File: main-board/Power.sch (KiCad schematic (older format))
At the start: 55 parts, among them J4 5V Input, Q1 N Channel, Q10 N Channel, Q11 N Channel, Q12 N Channel, Q13 P Channel, Q14 P Channel, Q15 P Channel, Q16 P Channel, Q17 P Channel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

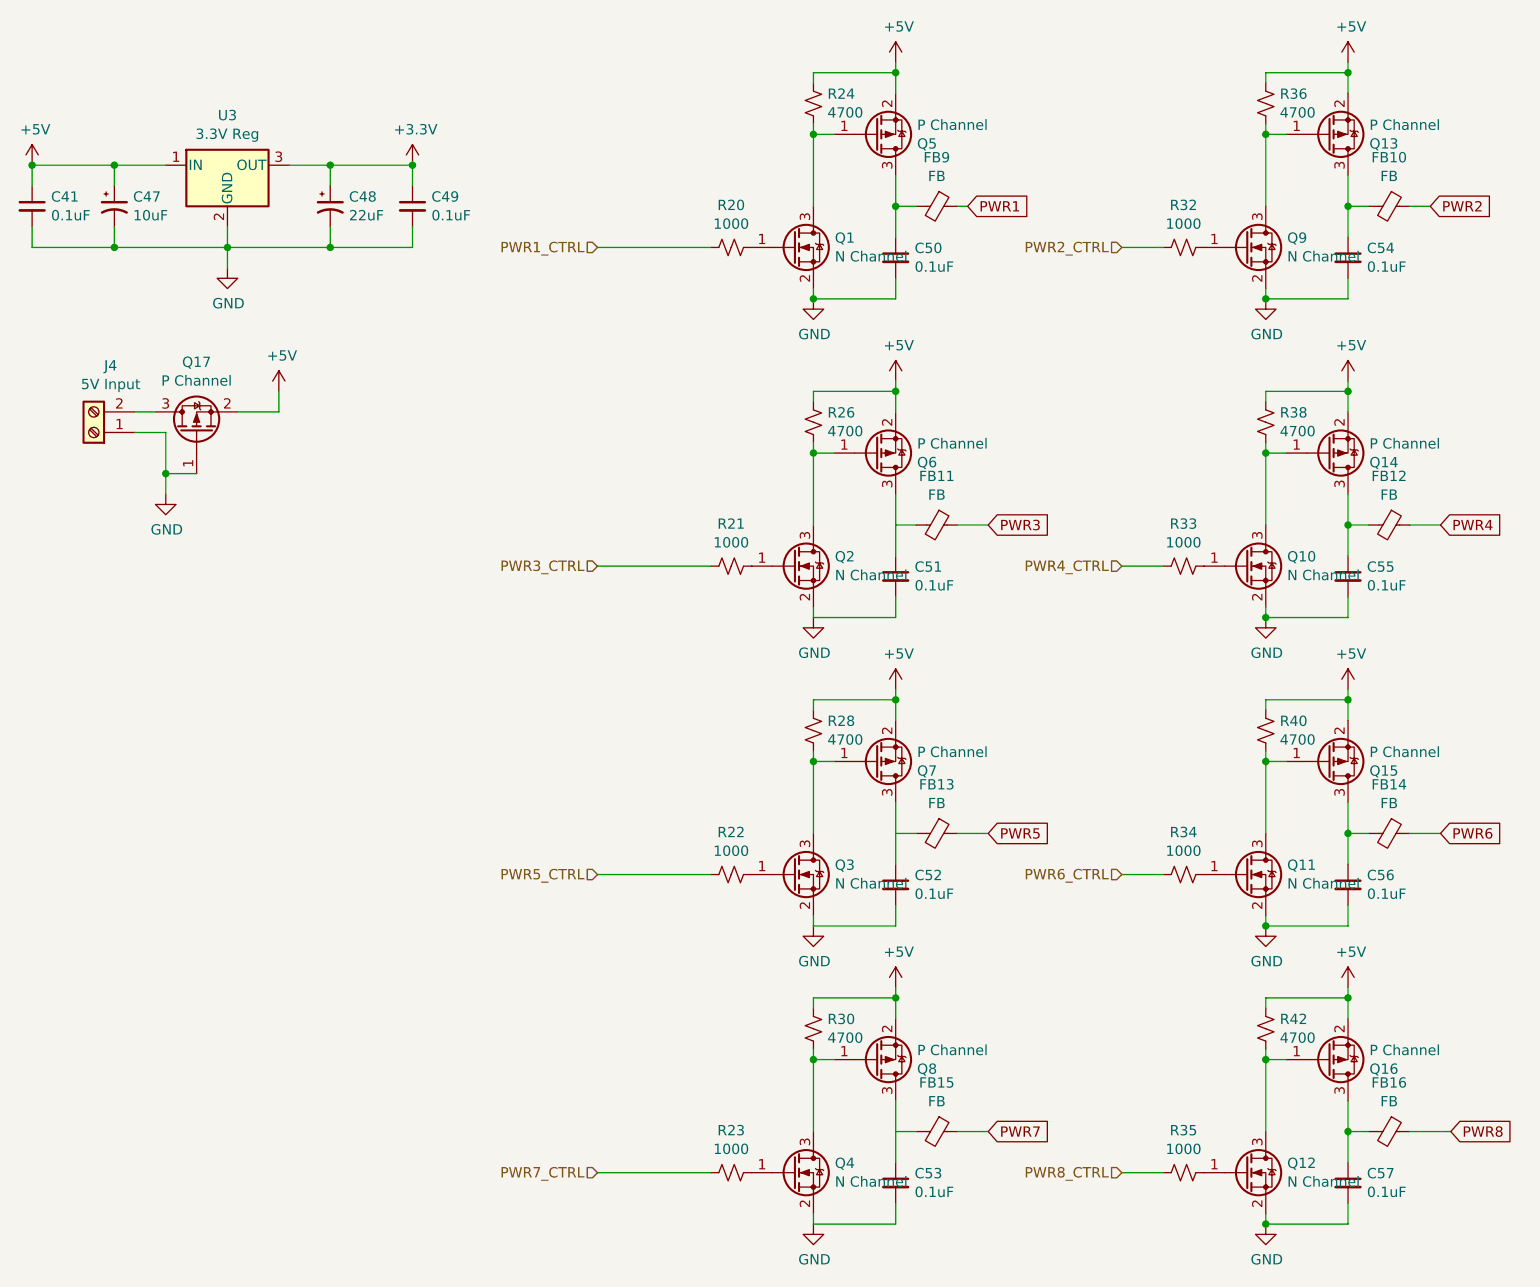
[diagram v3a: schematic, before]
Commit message: First round of rev 1 changes. This was a complete relayout.
* RS485 transceiver footprint fixed
* Compressed board to 100x100mm exactly
* Removed ethernet
* Changed FET footprints to SOT-23
* Swapped USB D+/D- to correct positions
* Spaced out +5V and GND silkscreen on power input
* Added JLCPCB order number silkscreen
* Spaced out Qwiic headers
* Added some more space around 3.3V regulator.
* Slightly increased size of electrolytic caps.
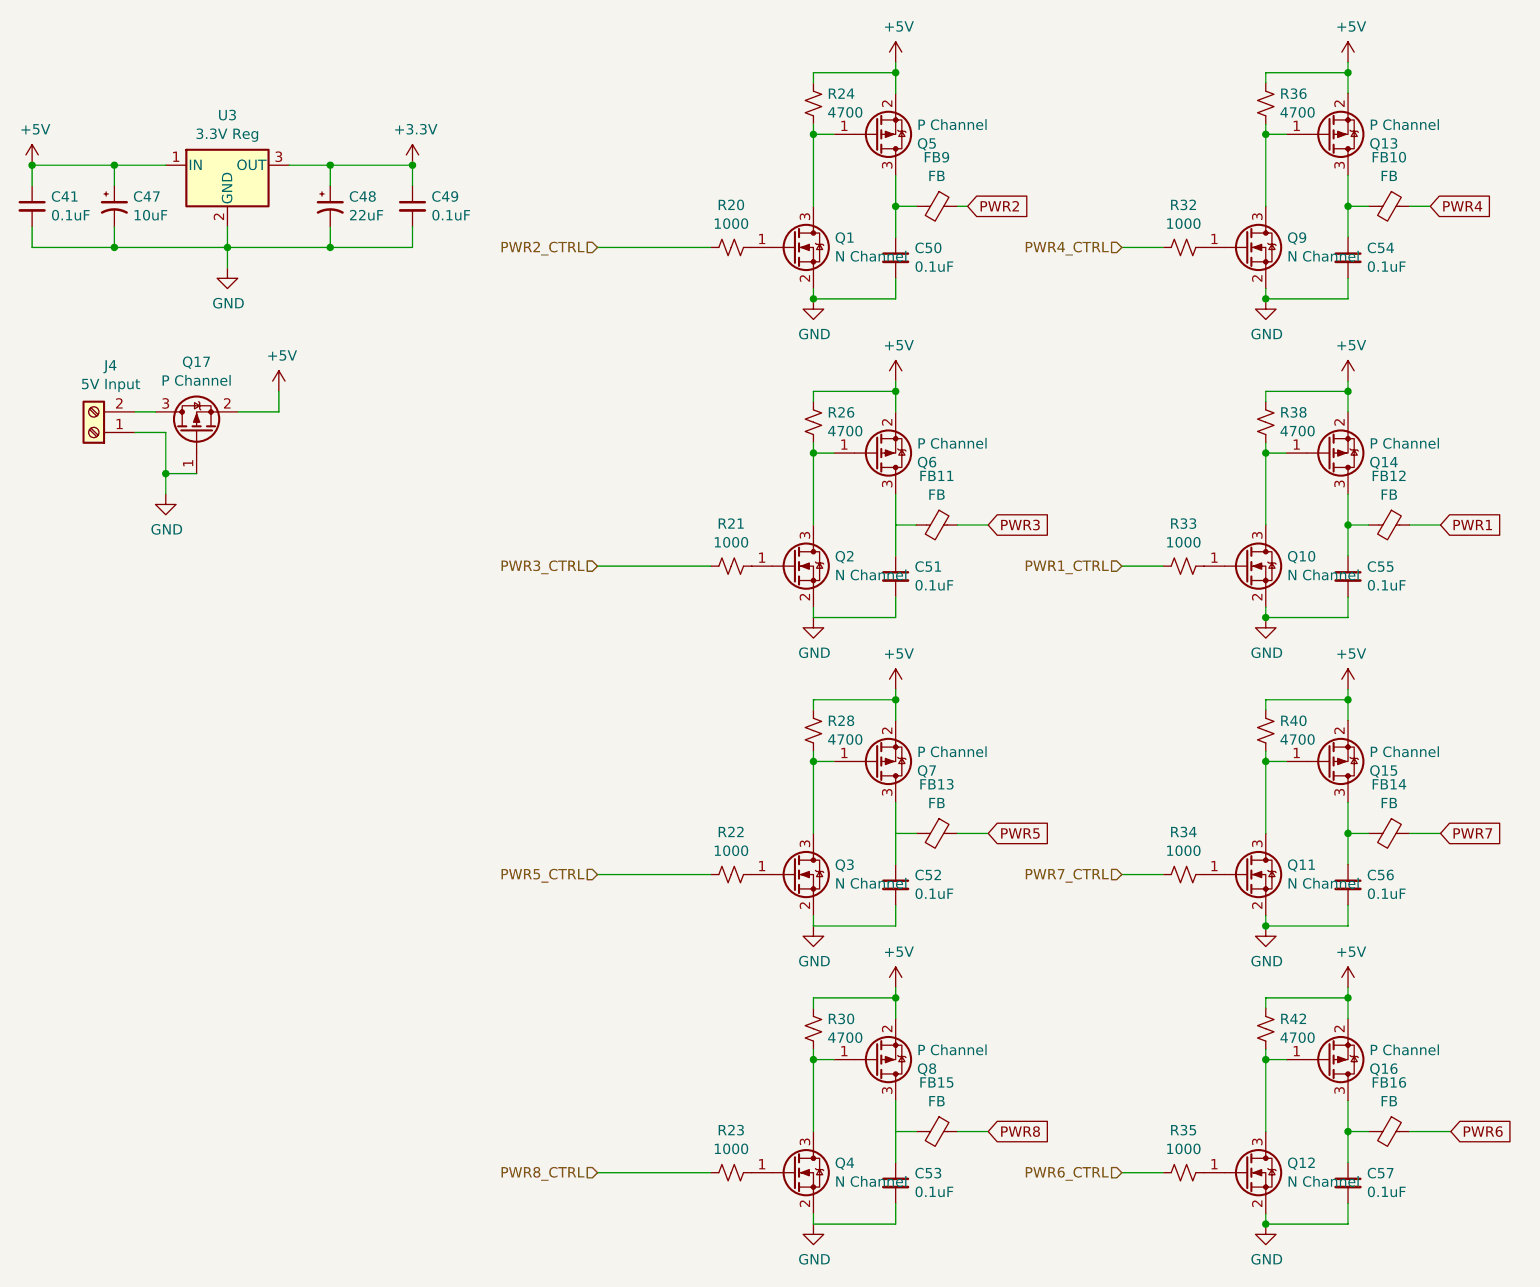
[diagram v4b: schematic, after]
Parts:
- C47: footprint Capacitors_SMD:CP_Elec_4x4.5 -> Capacitors_SMD:CP_Elec_5x5.3
- C48: footprint Capacitors_SMD:CP_Elec_5x5.3 -> Capacitors_SMD:CP_Elec_6.3x5.8
- Q1, Q10, Q11, Q12, Q13, Q14, Q15, Q16, Q17, Q2, Q3, Q4, Q5, Q6, Q7, Q8, Q9: footprint TO_SOT_Packages_SMD:SOT-323_SC-70_Handsoldering -> TO_SOT_Packages_SMD:SOT-23
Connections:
- net PWR1: now also FB12.1; no longer FB9.1
- net PWR1_CTRL: now also R33.2; no longer R20.2
- net PWR2: now also FB9.1; no longer FB10.1
- net PWR2_CTRL: now also R20.2; no longer R32.2
- net PWR4: now also FB10.1; no longer FB12.1
- net PWR4_CTRL: now also R32.2; no longer R33.2
- net PWR6: now also FB16.1; no longer FB14.1
- net PWR6_CTRL: now also R35.2; no longer R34.2
- net PWR7: now also FB14.1; no longer FB15.1
- net PWR7_CTRL: now also R34.2; no longer R23.2
- net PWR8: now also FB15.1; no longer FB16.1
- net PWR8_CTRL: now also R23.2; no longer R35.2
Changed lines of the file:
@@
 F 0 "C47" H 1341 1596 50  0000 L CNN
 F 1 "10uF" H 1341 1505 50  0000 L CNN
-F 2 "Capacitors_SMD:CP_Elec_4x4.5" H 1250 1550 50  0001 C CNN
+F 2 "Capacitors_SMD:CP_Elec_5x5.3" H 1250 1550 50  0001 C CNN
 F 3 "~" H 1250 1550 50  0001 C CNN
 	1    1250 1550
@@
 F 0 "C48" H 2391 1596 50  0000 L CNN
 F 1 "22uF" H 2391 1505 50  0000 L CNN
-F 2 "Capacitors_SMD:CP_Elec_5x5.3" H 2300 1550 50  0001 C CNN
+F 2 "Capacitors_SMD:CP_Elec_6.3x5.8" H 2300 1550 50  0001 C CNN
 F 3 "~" H 2300 1550 50  0001 C CNN
 	1    2300 1550
@@
 F 0 "Q1" H 4754 1796 50  0000 L CNN
 F 1 "N Channel" H 4754 1705 50  0000 L CNN
-F 2 "TO_SOT_Packages_SMD:SOT-323_SC-70_Handsoldering" H 4750 1850 50  0001 C CNN
+F 2 "TO_SOT_Packages_SMD:SOT-23" H 4750 1850 50  0001 C CNN
 F 3 "~" H 4550 1750 50  0001 C CNN
 	1    4550 1750
@@
 F 0 "Q5" H 5154 1246 50  0000 L CNN
 F 1 "P Channel" H 5154 1155 50  0000 L CNN
-F 2 "TO_SOT_Packages_SMD:SOT-323_SC-70_Handsoldering" H 5150 1300 50  0001 C CNN
+F 2 "TO_SOT_Packages_SMD:SOT-23" H 5150 1300 50  0001 C CNN
 F 3 "~" H 4950 1200 50  0001 C CNN
 	1    4950 1200
@@
 F 0 "Q9" H 6954 1796 50  0000 L CNN
 F 1 "N Channel" H 6954 1705 50  0000 L CNN
-F 2 "TO_SOT_Packages_SMD:SOT-323_SC-70_Handsoldering" H 6950 1850 50  0001 C CNN
+F 2 "TO_SOT_Packages_SMD:SOT-23" H 6950 1850 50  0001 C CNN
 F 3 "~" H 6750 1750 50  0001 C CNN
 	1    6750 1750
@@
 F 0 "Q13" H 7354 1246 50  0000 L CNN
 F 1 "P Channel" H 7354 1155 50  0000 L CNN
-F 2 "TO_SOT_Packages_SMD:SOT-323_SC-70_Handsoldering" H 7350 1300 50  0001 C CNN
+F 2 "TO_SOT_Packages_SMD:SOT-23" H 7350 1300 50  0001 C CNN
 F 3 "~" H 7150 1200 50  0001 C CNN
 	1    7150 1200
@@
 F 0 "Q2" H 4754 3346 50  0000 L CNN
 F 1 "N Channel" H 4754 3255 50  0000 L CNN
-F 2 "TO_SOT_Packages_SMD:SOT-323_SC-70_Handsoldering" H 4750 3400 50  0001 C CNN
+F 2 "TO_SOT_Packages_SMD:SOT-23" H 4750 3400 50  0001 C CNN
 F 3 "~" H 4550 3300 50  0001 C CNN
 	1    4550 3300
@@
 F 0 "Q6" H 5154 2796 50  0000 L CNN
 F 1 "P Channel" H 5154 2705 50  0000 L CNN
-F 2 "TO_SOT_Packages_SMD:SOT-323_SC-70_Handsoldering" H 5150 2850 50  0001 C CNN
+F 2 "TO_SOT_Packages_SMD:SOT-23" H 5150 2850 50  0001 C CNN
 F 3 "~" H 4950 2750 50  0001 C CNN
 	1    4950 2750
@@
 F 0 "Q10" H 6954 3346 50  0000 L CNN
 F 1 "N Channel" H 6954 3255 50  0000 L CNN
-F 2 "TO_SOT_Packages_SMD:SOT-323_SC-70_Handsoldering" H 6950 3400 50  0001 C CNN
+F 2 "TO_SOT_Packages_SMD:SOT-23" H 6950 3400 50  0001 C CNN
 F 3 "~" H 6750 3300 50  0001 C CNN
 	1    6750 3300
@@
 F 0 "Q14" H 7354 2796 50  0000 L CNN
 F 1 "P Channel" H 7354 2705 50  0000 L CNN
-F 2 "TO_SOT_Packages_SMD:SOT-323_SC-70_Handsoldering" H 7350 2850 50  0001 C CNN
+F 2 "TO_SOT_Packages_SMD:SOT-23" H 7350 2850 50  0001 C CNN
 F 3 "~" H 7150 2750 50  0001 C CNN
 	1    7150 2750
@@
 F 0 "Q3" H 4754 4846 50  0000 L CNN
 F 1 "N Channel" H 4754 4755 50  0000 L CNN
-F 2 "TO_SOT_Packages_SMD:SOT-323_SC-70_Handsoldering" H 4750 4900 50  0001 C CNN
+F 2 "TO_SOT_Packages_SMD:SOT-23" H 4750 4900 50  0001 C CNN
 F 3 "~" H 4550 4800 50  0001 C CNN
 	1    4550 4800
@@
 F 0 "Q7" H 5154 4296 50  0000 L CNN
 F 1 "P Channel" H 5154 4205 50  0000 L CNN
-F 2 "TO_SOT_Packages_SMD:SOT-323_SC-70_Handsoldering" H 5150 4350 50  0001 C CNN
+F 2 "TO_SOT_Packages_SMD:SOT-23" H 5150 4350 50  0001 C CNN
 F 3 "~" H 4950 4250 50  0001 C CNN
 	1    4950 4250
@@
 F 0 "Q11" H 6954 4846 50  0000 L CNN
 F 1 "N Channel" H 6954 4755 50  0000 L CNN
-F 2 "TO_SOT_Packages_SMD:SOT-323_SC-70_Handsoldering" H 6950 4900 50  0001 C CNN
+F 2 "TO_SOT_Packages_SMD:SOT-23" H 6950 4900 50  0001 C CNN
 F 3 "~" H 6750 4800 50  0001 C CNN
 	1    6750 4800
@@
 F 0 "Q15" H 7354 4296 50  0000 L CNN
 F 1 "P Channel" H 7354 4205 50  0000 L CNN
-F 2 "TO_SOT_Packages_SMD:SOT-323_SC-70_Handsoldering" H 7350 4350 50  0001 C CNN
+F 2 "TO_SOT_Packages_SMD:SOT-23" H 7350 4350 50  0001 C CNN
 F 3 "~" H 7150 4250 50  0001 C CNN
 	1    7150 4250
@@
 F 0 "Q4" H 4754 6296 50  0000 L CNN
 F 1 "N Channel" H 4754 6205 50  0000 L CNN
-F 2 "TO_SOT_Packages_SMD:SOT-323_SC-70_Handsoldering" H 4750 6350 50  0001 C CNN
+F 2 "TO_SOT_Packages_SMD:SOT-23" H 4750 6350 50  0001 C CNN
 F 3 "~" H 4550 6250 50  0001 C CNN
 	1    4550 6250
@@
 F 0 "Q8" H 5154 5746 50  0000 L CNN
 F 1 "P Channel" H 5154 5655 50  0000 L CNN
-F 2 "TO_SOT_Packages_SMD:SOT-323_SC-70_Handsoldering" H 5150 5800 50  0001 C CNN
+F 2 "TO_SOT_Packages_SMD:SOT-23" H 5150 5800 50  0001 C CNN
 F 3 "~" H 4950 5700 50  0001 C CNN
 	1    4950 5700
@@
 F 0 "Q12" H 6954 6296 50  0000 L CNN
 F 1 "N Channel" H 6954 6205 50  0000 L CNN
-F 2 "TO_SOT_Packages_SMD:SOT-323_SC-70_Handsoldering" H 6950 6350 50  0001 C CNN
+F 2 "TO_SOT_Packages_SMD:SOT-23" H 6950 6350 50  0001 C CNN
 F 3 "~" H 6750 6250 50  0001 C CNN
 	1    6750 6250
@@
 F 0 "Q16" H 7354 5746 50  0000 L CNN
 F 1 "P Channel" H 7354 5655 50  0000 L CNN
-F 2 "TO_SOT_Packages_SMD:SOT-323_SC-70_Handsoldering" H 7350 5800 50  0001 C CNN
+F 2 "TO_SOT_Packages_SMD:SOT-23" H 7350 5800 50  0001 C CNN
 F 3 "~" H 7150 5700 50  0001 C CNN
 	1    7150 5700
@@
 F 0 "Q17" V 1992 2650 50  0000 C CNN
 F 1 "P Channel" V 1901 2650 50  0000 C CNN
-F 2 "TO_SOT_Packages_SMD:SOT-323_SC-70_Handsoldering" H 1850 2750 50  0001 C CNN
+F 2 "TO_SOT_Packages_SMD:SOT-23" H 1850 2750 50  0001 C CNN
 F 3 "~" H 1650 2650 50  0001 C CNN
 	1    1650 2650
@@
 	1500 2850 1500 2950
 Text GLabel 5400 1550 2    50   Input ~ 0
-PWR1
+PWR2
 Wire Wire Line
 	5050 3100 5150 3100
@@
 	5050 6050 5150 6050
 Text GLabel 5500 6050 2    50   Input ~ 0
-PWR7
+PWR8
 Wire Wire Line
 	7250 6050 7350 6050
 Text GLabel 7750 6050 2    50   Input ~ 0
-PWR8
+PWR6
 Wire Wire Line
 	7250 4600 7350 4600
 Text GLabel 7700 4600 2    50   Input ~ 0
-PWR6
+PWR7
 Wire Wire Line
 	7250 3100 7350 3100
 Text GLabel 7700 3100 2    50   Input ~ 0
-PWR4
+PWR1
 Wire Wire Line
 	7250 1550 7350 1550
 Text GLabel 7650 1550 2    50   Input ~ 0
-PWR2
+PWR4
 $Comp
 L Device:Ferrite_Bead_Small FB?
@@
 	5050 6500 4650 6500
 Text HLabel 3600 1750 0    50   Input ~ 0
-PWR1_CTRL
+PWR2_CTRL
 Text HLabel 3600 3300 0    50   Input ~ 0
 PWR3_CTRL
 Text HLabel 6150 1750 0    50   Input ~ 0
-PWR2_CTRL
+PWR4_CTRL
 Text HLabel 6150 3300 0    50   Input ~ 0
-PWR4_CTRL
+PWR1_CTRL
 Text HLabel 6150 4800 0    50   Input ~ 0
-PWR6_CTRL
+PWR7_CTRL
 Text HLabel 3600 4800 0    50   Input ~ 0
 PWR5_CTRL
 Text HLabel 3600 6250 0    50   Input ~ 0
-PWR7_CTRL
+PWR8_CTRL
 Text HLabel 6150 6250 0    50   Input ~ 0
-PWR8_CTRL
+PWR6_CTRL
 Connection ~ 6850 2000
 Connection ~ 6850 3550
